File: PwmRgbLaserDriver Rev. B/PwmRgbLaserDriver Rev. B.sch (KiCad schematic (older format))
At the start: 56 parts

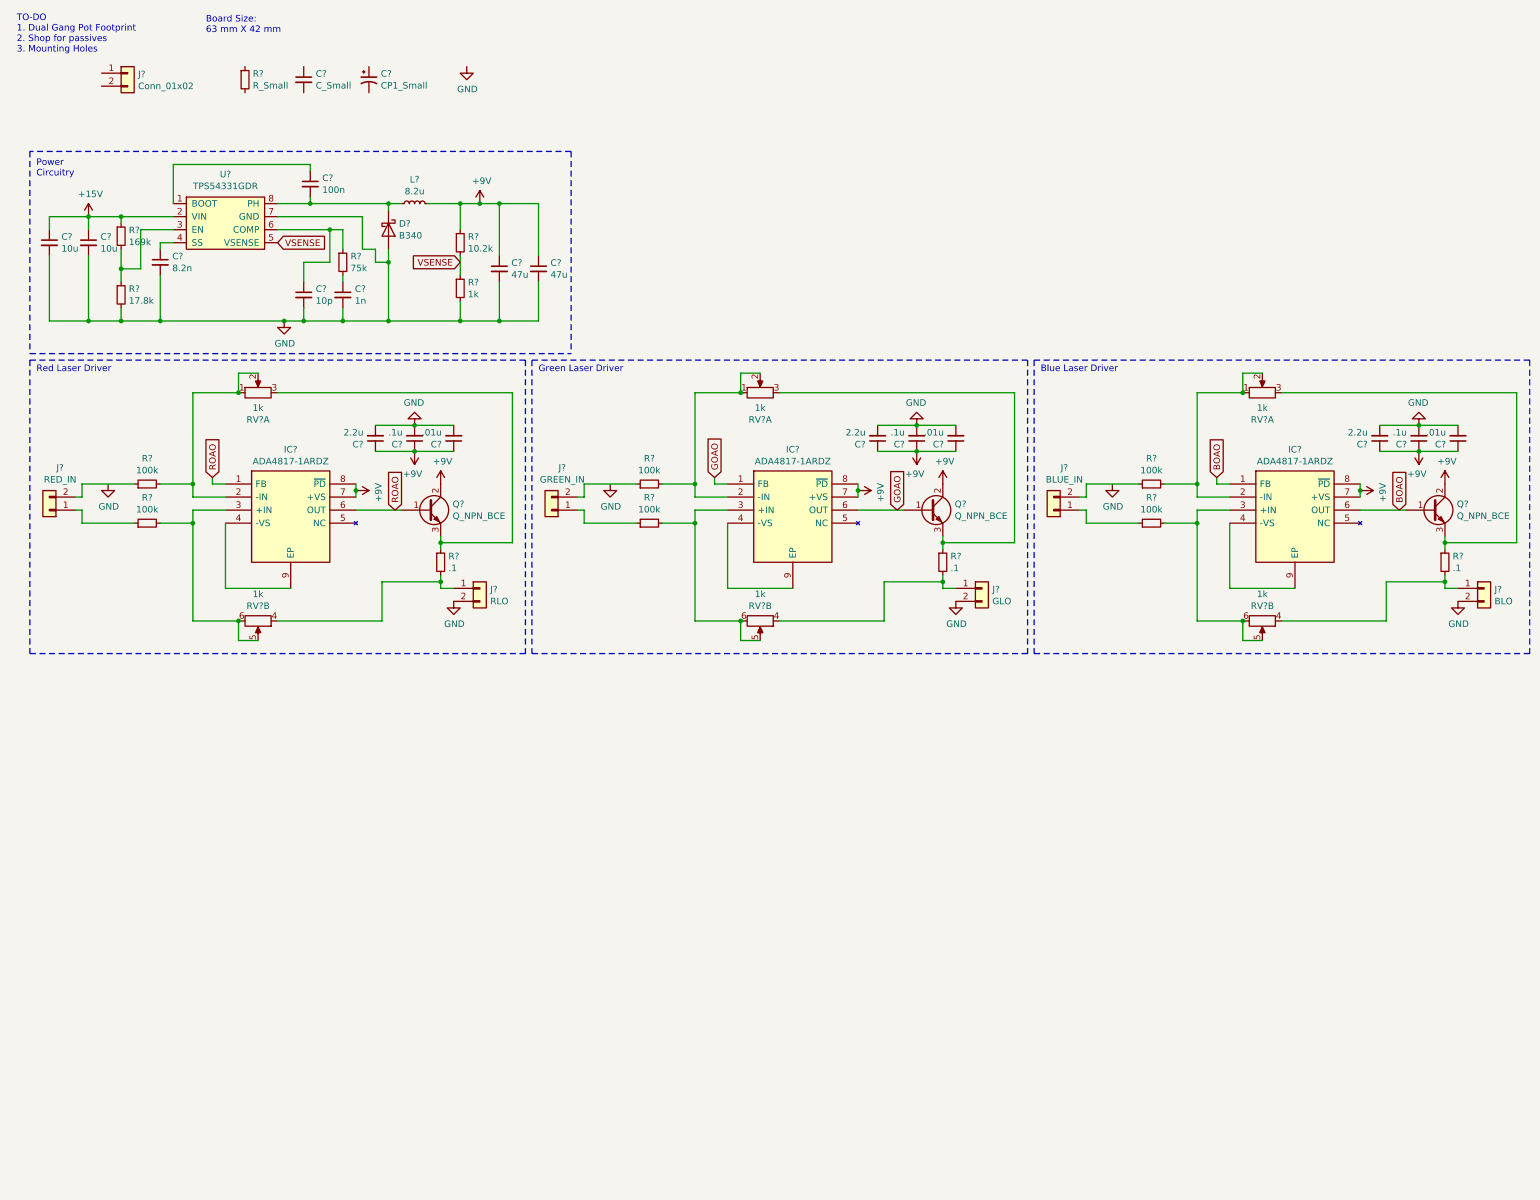
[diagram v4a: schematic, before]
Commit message: Some Footprints Added
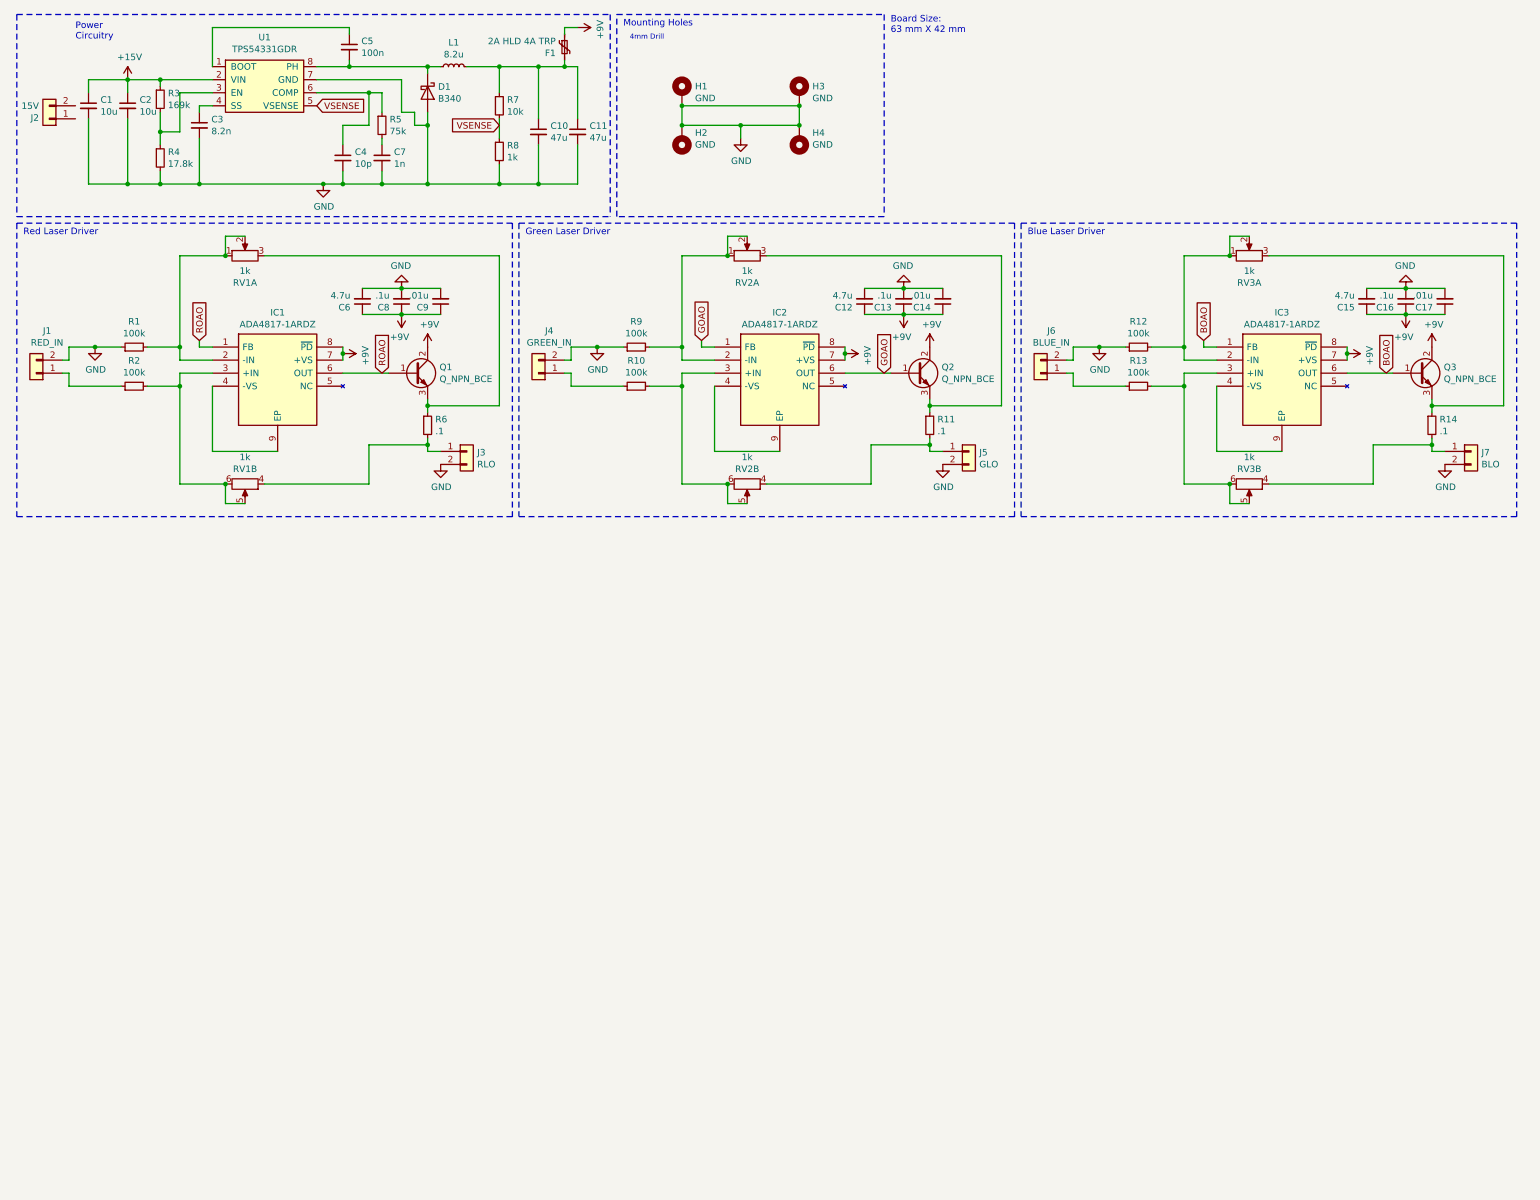
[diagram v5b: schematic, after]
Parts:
- removed C?: C_Small, symbol Device:C_Small
- removed C?: CP1_Small, symbol Device:CP1_Small
- removed R?: R_Small, symbol Device:R_Small
- added F1: 2A HLD 4A TRP, symbol Device:Polyfuse_Small
- added H1, H2, H3, H4: GND, symbol Mechanical:MountingHole_Pad
- C1, C2: renamed from C?; footprint (none) -> Capacitor_SMD:C_0805_2012Metric_Pad1.18x1.45mm_HandSolder
- C10, C11: renamed from C?; footprint (none) -> Capacitor_SMD:C_1210_3225Metric_Pad1.33x2.70mm_HandSolder
- C12, C15, C6: renamed from C?; value 2.2u -> 4.7u; footprint (none) -> Capacitor_SMD:C_0805_2012Metric_Pad1.18x1.45mm_HandSolder
- C13, C14, C16, C17, C3, C4, C5, C7, C8, C9: renamed from C?; footprint (none) -> Capacitor_SMD:C_0402_1005Metric_Pad0.74x0.62mm_HandSolder
- IC1, IC2, IC3: renamed from IC?; footprint SOIC127P600X175-9N -> SamacSys_Parts:SOIC127P600X175-9N
- J1, J3, J4, J5, J6, J7: renamed from J?; footprint (none) -> Connector_PinHeader_2.54mm:PinHeader_1x02_P2.54mm_Vertical
- J2: renamed from J?; value Conn_01x02 -> 15V; footprint (none) -> Connector_PinHeader_2.54mm:PinHeader_1x02_P2.54mm_Vertical
- R1, R10, R11, R12, R13, R14, R2, R3, R4, R5, R6, R9: renamed from R?; footprint (none) -> Resistor_SMD:R_0402_1005Metric_Pad0.72x0.64mm_HandSolder
- R7: renamed from R?; value 10.2k -> 10k; footprint (none) -> Resistor_SMD:R_0805_2012Metric_Pad1.20x1.40mm_HandSolder
- R8: renamed from R?; footprint (none) -> Resistor_SMD:R_0603_1608Metric_Pad0.98x0.95mm_HandSolder
- gave numbers to parts that had none: 9
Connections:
- net +9V: now also F1.1; no longer C10.1, C11.1, L1.2, R7.1
- net GND: now also J1.2 (Pin_2), J4.2 (Pin_2), J6.2 (Pin_2), R1.1, R12.1, R9.1, H1.1, H2.1, H3.1, H4.1
- new net: C10.1, C11.1, F1.2, L1.2, R7.1
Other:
- note added: "4mm Drill"
- note added: "Mounting Holes"
- note removed: "TO-DO\n1. Dual Gang Pot Footprint\n2. Shop for passives\n3. Mounting Holes\n"
- moved on the sheet: C1, C10, C11, C12, C13, C14, C15, C16, C17, C2, C3, C4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
